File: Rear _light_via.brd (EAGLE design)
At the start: 59.8 x 72.7 mm, 9 parts

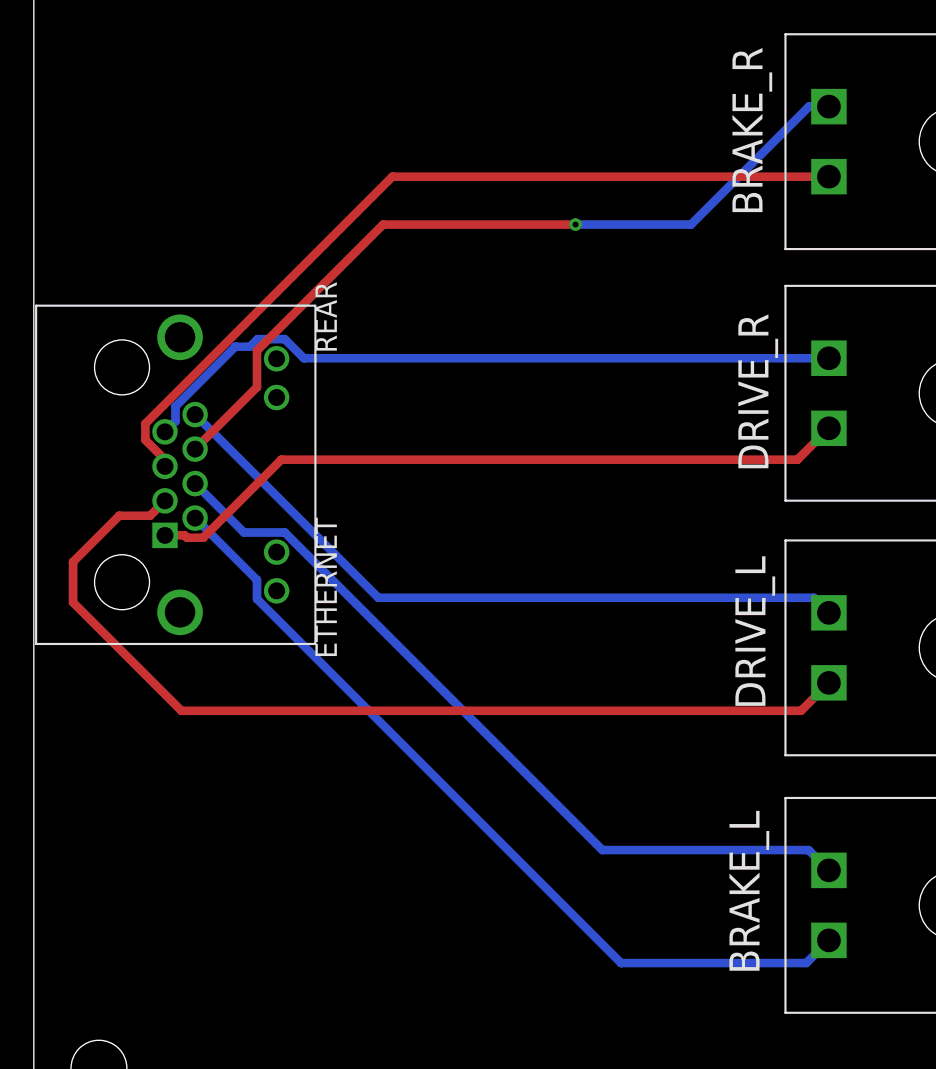
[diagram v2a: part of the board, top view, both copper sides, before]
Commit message: correct all routing errors
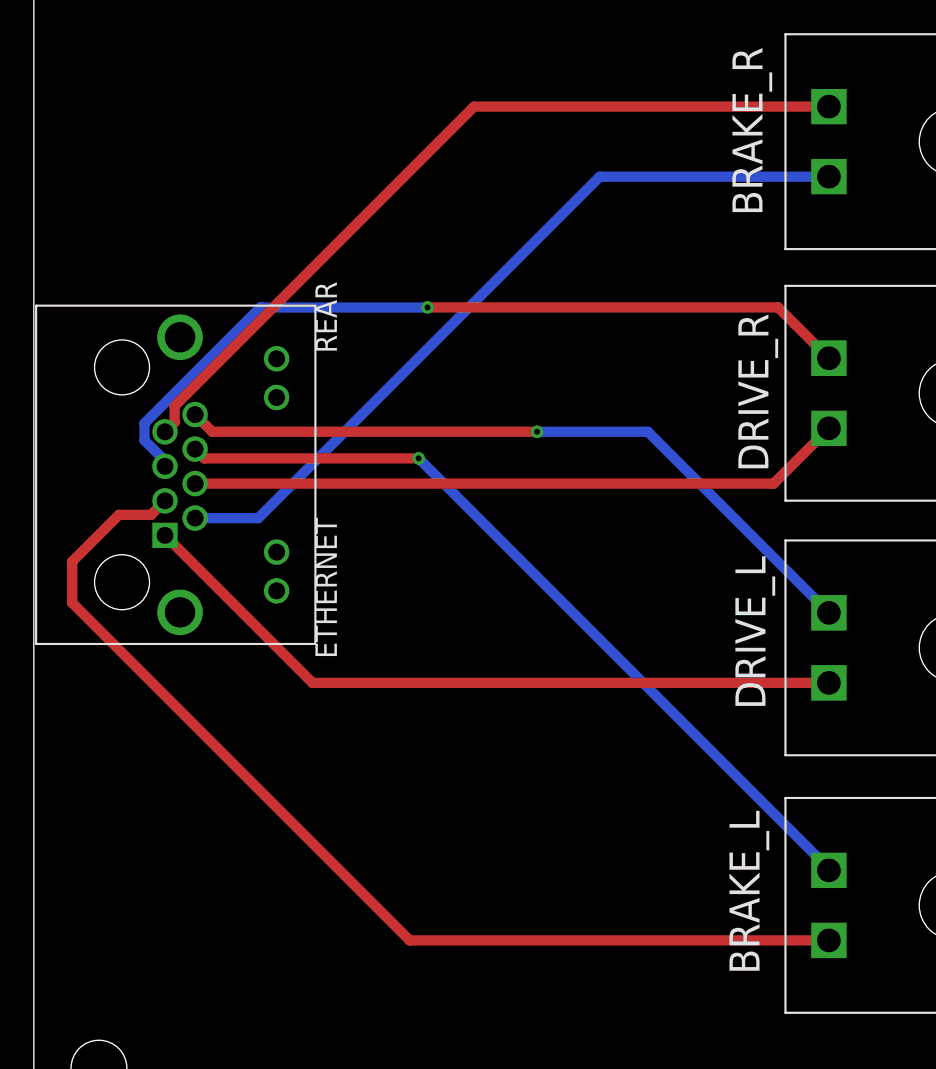
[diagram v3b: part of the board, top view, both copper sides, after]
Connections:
- net DRIVE_L renamed N$1
- removed net BRAKE_L: REAR.P$4, U$3.G/LOW
- removed net BRAKE_R: REAR.P$6, U$2.G/LOW
- removed net DRIVE_R: REAR.P$7, U$4.G/LOW
- removed net N$1 (its old number): REAR.P$1, U$4.V/SIG
- new net N$4: REAR.P$5, U$4.G/LOW
- new net N$5: REAR.P$4, U$4.V/SIG
- new net N$6: REAR.P$3, U$3.V/SIG
- new net N$8: REAR.P$1, U$1.V/SIG
- net N$2: now also REAR.P$7, U$2.G/LOW; no longer REAR.P$2, U$3.V/SIG
- net N$3: now also REAR.P$6, U$3.G/LOW; no longer REAR.P$5, U$2.V/SIG
- net N$7: now also REAR.P$2, U$2.V/SIG; no longer REAR.P$3, U$1.V/SIG
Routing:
- net N$6: track 0.00 -> 62.4 mm
- net N$4: track 0.00 -> 47.6 mm, vias 0 -> 1
- net BRAKE_R: track 47.1 -> 0.00 mm, vias 1 -> 0
- net BRAKE_L: track 46.9 -> 0.00 mm
- net N$8: track 0.00 -> 42.9 mm
- net DRIVE_R: track 42.5 -> 0.00 mm
- net N$1 (its old number): track 42.0 -> 0.00 mm
- net N$5: track 0.00 -> 38.8 mm
- net N$7: track 57.3 -> 45.8 mm
- net N$2: track 49.6 -> 47.8 mm
- net N$3: track 49.5 -> 47.8 mm, vias 0 -> 1
- net N$1: vias 0 -> 1
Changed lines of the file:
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@@
 <?xml version="1.0" encoding="utf-8"?>
 <!DOCTYPE eagle SYSTEM "eagle.dtd">
-<eagle version="8.6.1">
+<eagle version="9.0.0">
 <drawing>
 <settings>
@@
 <signals>
 <signal name="N$1">
+<contactref element="REAR" pad="P$8"/>
+<contactref element="U$1" pad="G/LOW"/>
+<wire x1="9.535" y1="42.49" x2="10.55" y2="41.475" width="0.6096" layer="1"/>
+<wire x1="10.55" y1="41.475" x2="29.75" y2="41.475" width="0.6096" layer="1"/>
+<via x="29.75" y="41.475" extent="1-16" drill="0.35"/>
+<wire x1="29.75" y1="41.475" x2="36.3" y2="41.475" width="0.6096" layer="16"/>
+<wire x1="36.3" y1="41.475" x2="47.005" y2="30.77" width="0.6096" layer="16"/>
+</signal>
+<signal name="N$2">
+<contactref element="U$2" pad="G/LOW"/>
+<contactref element="REAR" pad="P$7"/>
+<wire x1="7.755" y1="41.47" x2="8.3238" y2="42.0388" width="0.6096" layer="1"/>
+<wire x1="8.3238" y1="42.0388" x2="8.3238" y2="42.9917" width="0.6096" layer="1"/>
+<wire x1="8.3238" y1="42.9917" x2="26.0271" y2="60.695" width="0.6096" layer="1"/>
+<wire x1="26.0271" y1="60.695" x2="47.005" y2="60.695" width="0.6096" layer="1"/>
+</signal>
+<signal name="N$3">
+<contactref element="REAR" pad="P$6"/>
+<contactref element="U$3" pad="G/LOW"/>
+<wire x1="9.535" y1="40.45" x2="10.085" y2="39.9" width="0.6096" layer="1"/>
+<wire x1="10.085" y1="39.9" x2="22.75" y2="39.9" width="0.6096" layer="1"/>
+<via x="22.75" y="39.9" extent="1-16" drill="0.35"/>
+<wire x1="22.75" y1="39.9" x2="47.005" y2="15.645" width="0.6096" layer="16"/>
+<wire x1="47.005" y1="15.645" x2="47.005" y2="15.545" width="0.6096" layer="16"/>
+</signal>
+<signal name="N$4">
+<contactref element="REAR" pad="P$5"/>
+<contactref element="U$4" pad="G/LOW"/>
+<via x="23.275" y="48.825" extent="1-16" drill="0.35"/>
+<wire x1="6.5438" y1="40.9683" x2="6.5438" y2="41.9717" width="0.6096" layer="16"/>
+<wire x1="7.755" y1="39.43" x2="7.755" y2="39.7571" width="0.6096" layer="16"/>
+<wire x1="7.755" y1="39.7571" x2="6.5438" y2="40.9683" width="0.6096" layer="16"/>
+<wire x1="6.5438" y1="41.9717" x2="13.3971" y2="48.825" width="0.6096" layer="16"/>
+<wire x1="13.3971" y1="48.825" x2="23.275" y2="48.825" width="0.6096" layer="16"/>
+<wire x1="23.275" y1="48.825" x2="44" y2="48.825" width="0.6096" layer="1"/>
+<wire x1="44" y1="48.825" x2="47.005" y2="45.82" width="0.6096" layer="1"/>
+</signal>
+<signal name="N$5">
+<contactref element="REAR" pad="P$4"/>
+<contactref element="U$4" pad="V/SIG"/>
+<wire x1="9.535" y1="38.41" x2="43.735" y2="38.41" width="0.6096" layer="1"/>
+<wire x1="43.735" y1="38.41" x2="47.005" y2="41.68" width="0.6096" layer="1"/>
+</signal>
+<signal name="N$6">
+<contactref element="REAR" pad="P$3"/>
+<contactref element="U$3" pad="V/SIG"/>
+<wire x1="2.2692" y1="33.80019375" x2="2.2692" y2="31.35980625" width="0.6096" layer="1"/>
+<wire x1="7.755" y1="37.39" x2="6.9262" y2="36.5612" width="0.6096" layer="1"/>
+<wire x1="6.9262" y1="36.5612" x2="5.03020625" y2="36.5612" width="0.6096" layer="1"/>
+<wire x1="5.03020625" y1="36.5612" x2="2.2692" y2="33.80019375" width="0.6096" layer="1"/>
+<wire x1="2.2692" y1="31.35980625" x2="22.22400625" y2="11.405" width="0.6096" layer="1"/>
+<wire x1="22.22400625" y1="11.405" x2="47.005" y2="11.405" width="0.6096" layer="1"/>
+</signal>
+<signal name="N$7">
+<contactref element="REAR" pad="P$2"/>
+<contactref element="U$2" pad="V/SIG"/>
+<wire x1="9.535" y1="36.37" x2="13.27" y2="36.37" width="0.6096" layer="16"/>
+<wire x1="33.455" y1="56.555" x2="47.005" y2="56.555" width="0.6096" layer="16"/>
+<wire x1="13.27" y1="36.37" x2="33.455" y2="56.555" width="0.6096" layer="16"/>
+</signal>
+<signal name="N$8">
 <contactref element="REAR" pad="P$1"/>
-<wire x1="9.05434375" y1="35.2096" x2="10.01565625" y2="35.2096" width="0.508" layer="1"/>
-<wire x1="7.755" y1="35.35" x2="8.91394375" y2="35.35" width="0.508" layer="1"/>
-<wire x1="8.91394375" y1="35.35" x2="9.05434375" y2="35.2096" width="0.508" layer="1"/>
-<wire x1="10.01565625" y1="35.2096" x2="14.63105625" y2="39.825" width="0.508" layer="1"/>
-<contactref element="U$4" pad="V/SIG"/>
-<wire x1="14.63105625" y1="39.825" x2="45.15" y2="39.825" width="0.508" layer="1"/>
-<wire x1="45.15" y1="39.825" x2="47.005" y2="41.68" width="0.508" layer="1"/>
-</signal>
-<signal name="BRAKE_L">
-<contactref element="REAR" pad="P$4"/>
-<wire x1="9.535" y1="38.41" x2="12.4246" y2="35.5204" width="0.508" layer="16"/>
-<wire x1="12.4246" y1="35.5204" x2="14.83565625" y2="35.5204" width="0.508" layer="16"/>
-<wire x1="14.83565625" y1="35.5204" x2="33.61105625" y2="16.745" width="0.508" layer="16"/>
-<contactref element="U$3" pad="G/LOW"/>
-<wire x1="33.61105625" y1="16.745" x2="45.805" y2="16.745" width="0.508" layer="16"/>
-<wire x1="45.805" y1="16.745" x2="47.005" y2="15.545" width="0.508" layer="16"/>
-</signal>
-<signal name="BRAKE_R">
-<contactref element="REAR" pad="P$6"/>
-<via x="32.025" y="53.725" extent="1-16" drill="0.35"/>
-<wire x1="9.535" y1="40.45" x2="13.1946" y2="44.1096" width="0.508" layer="1"/>
-<wire x1="13.1946" y1="44.1096" x2="13.1946" y2="46.27065625" width="0.508" layer="1"/>
-<wire x1="13.1946" y1="46.27065625" x2="20.64894375" y2="53.725" width="0.508" layer="1"/>
-<wire x1="20.64894375" y1="53.725" x2="32.025" y2="53.725" width="0.508" layer="1"/>
-<wire x1="32.025" y1="53.725" x2="38.85" y2="53.725" width="0.508" layer="16"/>
-<contactref element="U$2" pad="G/LOW"/>
-<wire x1="38.85" y1="53.725" x2="45.82" y2="60.695" width="0.508" layer="16"/>
-<wire x1="45.82" y1="60.695" x2="47.005" y2="60.695" width="0.508" layer="16"/>
-</signal>
-<signal name="DRIVE_L">
-<contactref element="REAR" pad="P$8"/>
-<wire x1="9.535" y1="42.49" x2="20.365" y2="31.66" width="0.508" layer="16"/>
-<contactref element="U$1" pad="G/LOW"/>
-<wire x1="20.365" y1="31.66" x2="46.115" y2="31.66" width="0.508" layer="16"/>
-<wire x1="46.115" y1="31.66" x2="47.005" y2="30.77" width="0.508" layer="16"/>
-</signal>
-<signal name="N$2">
-<contactref element="REAR" pad="P$2"/>
-<wire x1="9.535" y1="36.37" x2="13.1946" y2="32.7104" width="0.508" layer="16"/>
-<wire x1="13.1946" y1="32.7104" x2="13.1946" y2="31.58934375" width="0.508" layer="16"/>
-<wire x1="13.1946" y1="31.58934375" x2="34.71894375" y2="10.065" width="0.508" layer="16"/>
-<contactref element="U$3" pad="V/SIG"/>
-<wire x1="34.71894375" y1="10.065" x2="45.665" y2="10.065" width="0.508" layer="16"/>
-<wire x1="45.665" y1="10.065" x2="47.005" y2="11.405" width="0.508" layer="16"/>
-</signal>
-<signal name="N$3">
-<contactref element="REAR" pad="P$5"/>
-<wire x1="6.5946" y1="40.98934375" x2="6.5946" y2="41.95065625" width="0.508" layer="1"/>
-<wire x1="7.755" y1="39.43" x2="7.755" y2="39.82894375" width="0.508" layer="1"/>
-<wire x1="7.755" y1="39.82894375" x2="6.5946" y2="40.98934375" width="0.508" layer="1"/>
-<contactref element="U$2" pad="V/SIG"/>
-<wire x1="21.19894375" y1="56.555" x2="47.005" y2="56.555" width="0.508" layer="1"/>
-<wire x1="6.5946" y1="41.95065625" x2="21.19894375" y2="56.555" width="0.508" layer="1"/>
-</signal>
-<signal name="DRIVE_R">
-<contactref element="REAR" pad="P$7"/>
-<wire x1="7.755" y1="41.47" x2="8.3746" y2="42.0896" width="0.508" layer="16"/>
-<wire x1="8.3746" y1="42.0896" x2="8.3746" y2="42.97065625" width="0.508" layer="16"/>
-<wire x1="11.90894375" y1="46.505" x2="12.79" y2="46.505" width="0.508" layer="16"/>
-<wire x1="12.79" y1="46.505" x2="13.2354" y2="46.9504" width="0.508" layer="16"/>
-<wire x1="8.3746" y1="42.97065625" x2="11.90894375" y2="46.505" width="0.508" layer="16"/>
-<wire x1="13.2354" y1="46.9504" x2="14.83565625" y2="46.9504" width="0.508" layer="16"/>
-<contactref element="U$4" pad="G/LOW"/>
-<wire x1="15.96605625" y1="45.82" x2="47.005" y2="45.82" width="0.508" layer="16"/>
-<wire x1="14.83565625" y1="46.9504" x2="15.96605625" y2="45.82" width="0.508" layer="16"/>
-</signal>
-<signal name="N$7">
-<contactref element="REAR" pad="P$3"/>
-<wire x1="2.32" y1="33.77915" x2="2.32" y2="31.38085" width="0.508" layer="1"/>
-<wire x1="7.755" y1="37.39" x2="6.8754" y2="36.5104" width="0.508" layer="1"/>
-<wire x1="6.8754" y1="36.5104" x2="5.05125" y2="36.5104" width="0.508" layer="1"/>
-<wire x1="5.05125" y1="36.5104" x2="2.32" y2="33.77915" width="0.508" layer="1"/>
-<wire x1="2.32" y1="31.38085" x2="8.72085" y2="24.98" width="0.508" layer="1"/>
 <contactref element="U$1" pad="V/SIG"/>
-<wire x1="8.72085" y1="24.98" x2="45.355" y2="24.98" width="0.508" layer="1"/>
-<wire x1="45.355" y1="24.98" x2="47.005" y2="26.63" width="0.508" layer="1"/>
+<wire x1="7.755" y1="35.35" x2="16.475" y2="26.63" width="0.6096" layer="1"/>
+<wire x1="16.475" y1="26.63" x2="47.005" y2="26.63" width="0.6096" layer="1"/>
 </signal>
 </signals>
